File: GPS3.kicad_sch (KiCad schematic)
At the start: 12 parts, among them J3 GPS_ANT_0, U3 MAX-M10S-00B

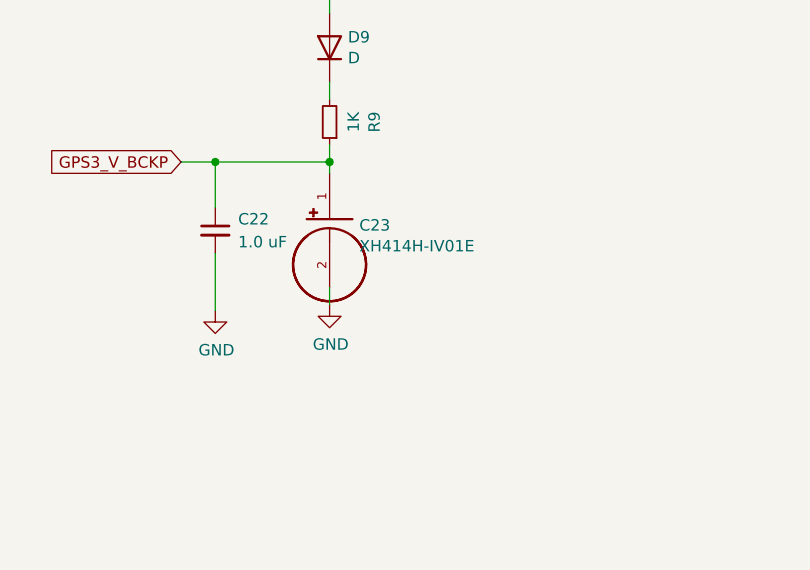
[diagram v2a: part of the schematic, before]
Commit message: Corrected battery position
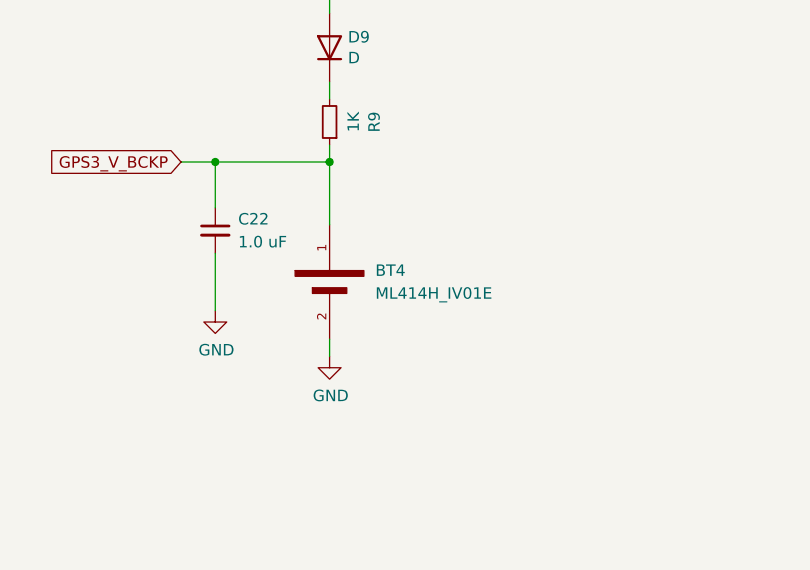
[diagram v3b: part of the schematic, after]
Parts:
- removed C23: XH414H-IV01E, XH414H:CAP_XH414H-IV01E, symbol XH414H-IV01E:XH414H-IV01E
- added BT4: ML414H_IV01E, ML414H_IV01E:SEIKO_ML414H_IV01E, symbol ML414H_IV01E:ML414H_IV01E
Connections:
- net GND: now also BT4.2
- net GPS3_V_BCKP: now also BT4.1
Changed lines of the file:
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@@
     (stroke (width 0) (type default) (color 0 0 0 0))
   )
-  (wire (pts (xy 126.365 154.305) (xy 126.365 156.21))
+  (wire (pts (xy 126.365 160.02) (xy 126.365 161.925))
     (stroke (width 0) (type default) (color 0 0 0 0))
   )
@@
     (stroke (width 0) (type default) (color 0 0 0 0))
   )
-  (wire (pts (xy 126.365 140.335) (xy 126.365 141.605))
+  (wire (pts (xy 126.365 140.335) (xy 126.365 147.32))
     (stroke (width 0) (type default) (color 0 0 0 0))
   )
@@
     (pin "1")
   )
+  (symbol (lib_id "ML414H_IV01E:ML414H_IV01E") (at 126.365 152.4 270) (unit 1)
+    (in_bom yes) (on_board yes) (fields_autoplaced)
+    (property "Reference" "BT4" (id 0) (at 131.445 152.3999 90)
+      (effects (font (size 1.27 1.27)) (justify left))
+    )
+    (property "Value" "ML414H_IV01E" (id 1) (at 131.445 154.9399 90)
+      (effects (font (size 1.27 1.27)) (justify left))
+    )
+    (property "Footprint" "ML414H_IV01E:SEIKO_ML414H_IV01E" (id 2) (at 126.365 152.4 0)
+      (effects (font (size 1.27 1.27)) (justify bottom) hide)
+    )
+    (property "Datasheet" "" (id 3) (at 126.365 152.4 0)
+      (effects (font (size 1.27 1.27)) hide)
+    )
+    (property "STANDARD" "Manufacturer Recommendation" (id 4) (at 126.365 152.4 0)
+      (effects (font (size 1.27 1.27)) (justify bottom) hide)
+    )
+    (property "MANUFACTURER" "SEIKO" (id 5) (at 126.365 152.4 0)
+      (effects (font (size 1.27 1.27)) (justify bottom) hide)
+    )
+    (pin "1")
+    (pin "2")
+  )
   (symbol (lib_id "Device:R_Small") (at 126.365 135.89 180) (unit 1)
     (in_bom yes) (on_board yes)
@@
     (pin "2")
   )
-  (symbol (lib_id "power:GND") (at 126.365 156.21 0) (unit 1)
-    (in_bom yes) (on_board yes)
-    (property "Reference" "#PWR096" (id 0) (at 126.365 162.56 0)
-      (effects (font (size 1.27 1.27)) hide)
-    )
-    (property "Value" "GND" (id 1) (at 126.492 160.6042 0))
-    (property "Footprint" "" (id 2) (at 126.365 156.21 0)
-      (effects (font (size 1.27 1.27)) hide)
-    )
-    (property "Datasheet" "" (id 3) (at 126.365 156.21 0)
+  (symbol (lib_id "power:GND") (at 126.365 161.925 0) (unit 1)
+    (in_bom yes) (on_board yes)
+    (property "Reference" "#PWR096" (id 0) (at 126.365 168.275 0)
+      (effects (font (size 1.27 1.27)) hide)
+    )
+    (property "Value" "GND" (id 1) (at 126.492 166.3192 0))
+    (property "Footprint" "" (id 2) (at 126.365 161.925 0)
+      (effects (font (size 1.27 1.27)) hide)
+    )
+    (property "Datasheet" "" (id 3) (at 126.365 161.925 0)
       (effects (font (size 1.27 1.27)) hide)
     )
@@
     (pin "1")
   )
-  (symbol (lib_id "XH414H-IV01E:XH414H-IV01E") (at 126.365 146.685 0) (unit 1)
-    (in_bom yes) (on_board yes)
-    (property "Reference" "C23" (id 0) (at 129.667 147.3708 0)
-      (effects (font (size 1.27 1.27)) (justify left))
-    )
-    (property "Value" "XH414H-IV01E" (id 1) (at 129.667 149.6822 0)
-      (effects (font (size 1.27 1.27)) (justify left))
-    )
-    (property "Footprint" "XH414H:CAP_XH414H-IV01E" (id 2) (at 126.365 146.685 0)
-      (effects (font (size 1.27 1.27)) (justify left bottom) hide)
-    )
-    (property "Datasheet" "" (id 3) (at 126.365 146.685 0)
-      (effects (font (size 1.27 1.27)) (justify left bottom) hide)
-    )
-    (property "MANUFACTURER" "Seiko" (id 4) (at 126.365 146.685 0)
-      (effects (font (size 1.27 1.27)) (justify left bottom) hide)
-    )
-    (pin "1")
-    (pin "2")
-  )
   (symbol (lib_id "Device:C_Small") (at 36.83 62.23 0) (unit 1)

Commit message: Last commit
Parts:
- removed D9: D, Diode_SMD:D_1206_3216Metric_Pad1.42x1.75mm_HandSolder, symbol Device:D
- added D6: B0520LW-7-F, B0520LW-7-F:SOD3716X145N, symbol B0520LW-7-F:B0520LW-7-F
- C24: value 1uF -> 10uF; footprint Capacitor_Tantalum_SMD:CP_EIA-3528-21_Kemet-B_Pad1.50x2.35mm_HandSolder -> Capacitor_SMD:C_1210_3225Metric
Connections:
- net +3.3V: now also U3.7 (V_IO), D6.2 (A)
- net GND: no longer U3.7 (V_IO)
- net at R9.2: now also D6.1 (K)
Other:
- moved on the sheet: BT4, C22, C24, C9, J3, L4, R7, R9, U3
